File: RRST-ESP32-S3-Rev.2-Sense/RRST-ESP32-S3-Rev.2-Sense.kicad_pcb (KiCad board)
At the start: 4 copper layers, 20.1 x 39.9 mm, 35 parts, among them J1 USB_C_Receptacle_USB2.0_16P, J4 Conn_01x05_Socket, J5 Conn_01x02_Socket, J6 Conn_01x02_Socket, SW1 SW_Push, SW2 SW_Push, U1 LD1117S33TR_SOT223, U2 ESP32-S3-WROOM-1, U3 MCP2561-E-SN

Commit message: 自動配線前
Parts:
- removed CAN_BUS1, CAN_BUS2: Conn_01x04_Socket, Connector_JST:JST_GH_SM04B-GHS-TB_1x04-1MP_P1.25mm_Horizontal
- removed D7: LED, LED_SMD:LED_0603_1608Metric
- removed J4: Conn_01x05_Socket, Connector_PinSocket_2.54mm:PinSocket_1x05_P2.54mm_Horizontal
- removed R8: 0, Resistor_SMD:R_0603_1608Metric
- removed U3: MCP2561-E-SN, Package_SO:SOIC-8_3.9x4.9mm_P1.27mm
- added D8: LESD5D5.0CT1G, Diode_SMD:D_SOD-523, F.Cu at (80.6, 121.0)
- added G***: LOGO, LOGO, F.Cu at (52.1, 109.2)
- added G***: LOGO, LOGO, F.Cu at (52.1, 105.7)
- added G***: LOGO, LOGO, B.Cu at (86.2, 106.7)
- added G***: LOGO, LOGO, B.Cu at (79.1, 104.5)
- added J2: USB_C_Receptacle_USB2.0_16P, Connector_USB:USB_C_Receptacle_XKB_U262-16XN-4BVC11, F.Cu at (81.9, 131.6)
- added J3: Conn_01x22_Pin, Connector_PinHeader_2.54mm:PinHeader_1x22_P2.54mm_Vertical, B.Cu at (96.5, 78.7)
- added J7: Conn_01x04_Socket, Connector_PinHeader_2.54mm:PinHeader_1x04_P2.54mm_Vertical, F.Cu at (86.4, 116.0)
- added U4: MCP2561-E-SN, Package_SO:SOIC-8_3.9x4.9mm_P1.27mm, F.Cu at (80.2, 116.3)
- added ↓TERM: 0, Resistor_SMD:R_0805_2012Metric, F.Cu at (91.6, 105.5)
- C1: value 1uF -> 10uF
- C3: value 10uF -> 100nF
- C5: value 100nF -> 10uF
- C9: value 10uF -> 1uF
- D1: value SS14 -> LED; footprint Diode_SMD:D_SMA -> LED_SMD:LED_0603_1608Metric; moved to F.Cu
- D2: value LED -> SS14; footprint LED_SMD:LED_0603_1608Metric -> Diode_SMD:D_SMA
- D4: value LESD5D5.0CT1G -> LED; footprint Diode_SMD:D_SOD-523 -> LED_SMD:LED_0603_1608Metric
- J1: value USB_C_Receptacle_USB2.0_16P -> Conn_01x22_Pin; footprint Connector_USB:USB_C_Receptacle_XKB_U262-16XN-4BVC11 -> Connector_PinHeader_2.54mm:PinHeader_1x22_P2.54mm_Vertical; moved to B.Cu
- J5, J6: value Conn_01x02_Socket -> Conn_01x04_Socket; footprint Connector_JST:JST_PH_S2B-PH-K_1x02_P2.00mm_Horizontal -> Connector_JST:JST_XH_B4B-XH-A_1x04_P2.50mm_Vertical
- R1: value 10k -> 5.1k
- R3: value 5.1k -> 5.1K
- R5: value 5.1K -> 10k
- U1: value LD1117S33TR_SOT223 -> ESP32-S3-WROOM-1; footprint Package_TO_SOT_SMD:SOT-223-3_TabPin2 -> RF_Module:ESP32-S3-WROOM-1; moved to F.Cu
- U2: value ESP32-S3-WROOM-1 -> LD1117S33TR_SOT223; footprint RF_Module:ESP32-S3-WROOM-1 -> Package_TO_SOT_SMD:SOT-223-3_TabPin2
- moved R2 94.4 mm to (77.5, 104.9)
- moved C7 94.2 mm to (76.5, 101.1), turned to 90 degrees
- moved R1 92.5 mm to (77.5, 112.8)
- moved C5 92.4 mm to (77.5, 98.3)
- moved R4 91.4 mm to (82.1, 123.7), turned to -90 degrees
- moved R6 91.3 mm to (85.1, 98.3), turned to 180 degrees
- moved R5 90.6 mm to (84.6, 101.1), turned to -90 degrees
- moved C6 90.1 mm to (80.8, 98.3)
- moved R7 89.7 mm to (83.6, 123.8), turned to -90 degrees
- moved C4 89.6 mm to (77.5, 106.4), turned to 180 degrees
- moved C3 88.9 mm to (77.5, 107.9), turned to 180 degrees
- moved R3 88.8 mm to (80.6, 123.8), turned to -90 degrees
- moved C2 88.3 mm to (77.5, 109.4), turned to 180 degrees
- moved C1 87.9 mm to (77.5, 110.9), turned to 180 degrees
- moved C9 85.8 mm to (86.1, 101.1), turned to -90 degrees
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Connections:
- C1 pad 1: EN -> +5V
- C2 pad 1: EN -> +5V
- C4 pad 1: +5V -> 3V3
- C5 pad 1: IO0 -> 3V3
- C7 pad 1: +5V -> EN
- C8 pad 1: 3V3 -> IO0
- C9 pad 1: 3V3 -> EN
- D1 pad 1: +5V -> Net-(D1-K)
- D1 pad 2: VBUS -> 3V3
- D2 pad 1: GND -> +5V
- D2 pad 2: Net-(D2-A) -> VBUS
- D4 pad 1: VBUS -> GND
- D4 pad 2: GND -> Net-(D4-A)
- D5 pad 1: DN -> VBUS
- D6 pad 1: DP -> DN
- J5 pad 1: GPIO35 -> +5V
- J6 pad 1: GPIO36 -> +5V
- R1 pad 1: 3V3 -> +5V
- R1 pad 2: EN -> Net-(D3-A)
- R2 pad 1: +5V -> 3V3
- R2 pad 2: Net-(D2-A) -> Net-(D4-A)
- R3 pad 1: 3V3 -> Net-(J2-CC2)
- R3 pad 2: Net-(D3-A) -> GND
- R4 pad 1: Net-(J1-CC2) -> Net-(J2-CC1)
- R5 pad 1: Net-(J1-CC1) -> 3V3
- R5 pad 2: GND -> EN
- R6 pad 1: Net-(D7-K) -> Net-(D1-K)
- U1 pad 3: +5V -> EN
- U2 pad 3: EN -> +5V
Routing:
- net 3V3: track 0.00 -> 59.6 mm, vias 0 -> 2
- net GND: track 0.00 -> 54.7 mm, vias 0 -> 2
- net +5V: track 0.00 -> 24.4 mm
- net VBUS: track 0.00 -> 14.4 mm
- net DN: track 0.00 -> 3.06 mm
- net DP: track 0.00 -> 2.88 mm
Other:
- board size 20.1 x 39.9 mm -> 25.4 x 56.9 mm
- copper layers 4 -> 2
- board text added: "0"
- board text added: "1"
- board text added: "10"
- board text added: "11"
- board text added: "12"
- board text added: "13"
- board text added: "14"
- board text added: "15"
- board text added: "16"
- board text added: "17"
- board text added: "18"
- board text added: "19"
- board text added: "2"
- board text added: "20"
- board text added: "21"
- board text added: "3"
- board text added: "3.3V"
- board text added: "35"
- board text added: "36"
- board text added: "37"
- board text added: "38"
- board text added: "39"
- board text added: "3V3"
- board text added: "4"
- board text added: "40"
- board text added: "41"
- board text added: "42"
- board text added: "43"
- board text added: "44"
- board text added: "45"
- board text added: "46"
- board text added: "47"
- board text added: "48"
- board text added: "5"
- board text added: "5V"
- board text added: "6"
- board text added: "7"
- board text added: "8"
- board text added: "9"
- board text added: "BOOT"
- board text added: "GND"
- board text added: "RESET"
- board text added: "RRST-ESP32-S3 Rev.1 2026, NHK-Project, RRST"
- board text added: "RST"
- board text added: "RUN~"

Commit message: 自動配線&未配線の手直し完了
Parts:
- moved J6 0.09 mm to (91.1, 130.7)
- moved J5 0.09 mm to (91.1, 117.0)
- renumbered G*** to G***_1, G*** to G***_2, G*** to G***_3, G*** to G***_4
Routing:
- net CAN_TX: track 0.00 -> 76.0 mm, vias 0 -> 2
- net CAN_RX: track 0.00 -> 66.0 mm
- net DP: track 2.88 -> 68.1 mm, vias 0 -> 3
- net DN: track 3.06 -> 66.4 mm, vias 0 -> 3
- net +5V: track 24.4 -> 67.6 mm, vias 0 -> 1
- net IO14: track 0.00 -> 43.2 mm, vias 0 -> 2
- net IO13: track 0.00 -> 42.2 mm, vias 0 -> 1
- net EN: track 0.00 -> 39.0 mm, vias 0 -> 1
- net IO21: track 0.00 -> 38.9 mm, vias 0 -> 1
- net 3V3: track 59.6 -> 97.9 mm
- net Net-(R7-Pad1): track 0.00 -> 31.8 mm, vias 0 -> 2
- net IO12: track 0.00 -> 31.2 mm, vias 0 -> 1
- net IO10: track 0.00 -> 30.8 mm, vias 0 -> 1
- net IO0: track 0.00 -> 30.7 mm
- net IO11: track 0.00 -> 29.8 mm, vias 0 -> 2
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- added copper zone on B.Cu, net GND
- added copper zone on F.Cu, net GND
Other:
- copper layers 2 -> 4
- board text added: "RRST-ESP32-S3 Rev.2 Sense 2026, NHK-Project, RRST"
- board text added: "RUN"
- board text removed: "RRST-ESP32-S3 Rev.1 2026, NHK-Project, RRST"
- board text removed: "RUN~"

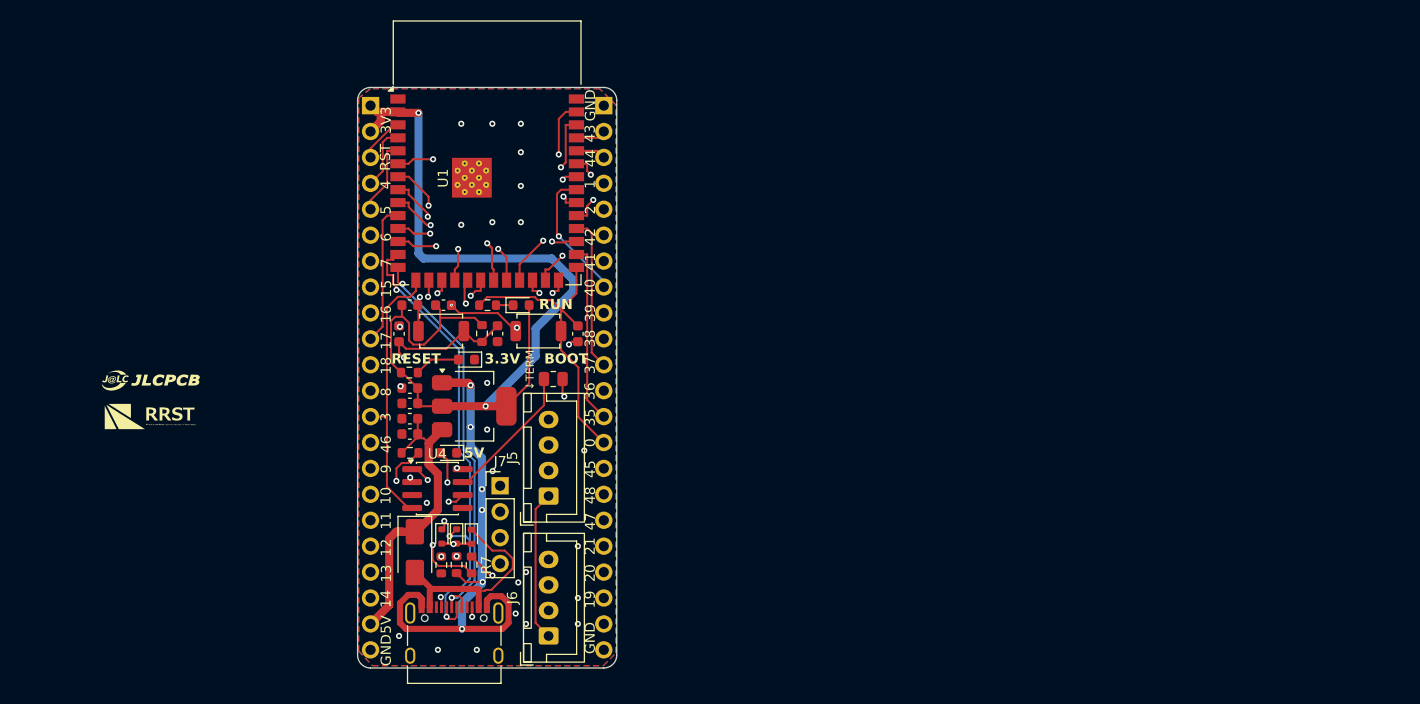
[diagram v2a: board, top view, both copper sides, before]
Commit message: マイコンにセンサ入力を増設
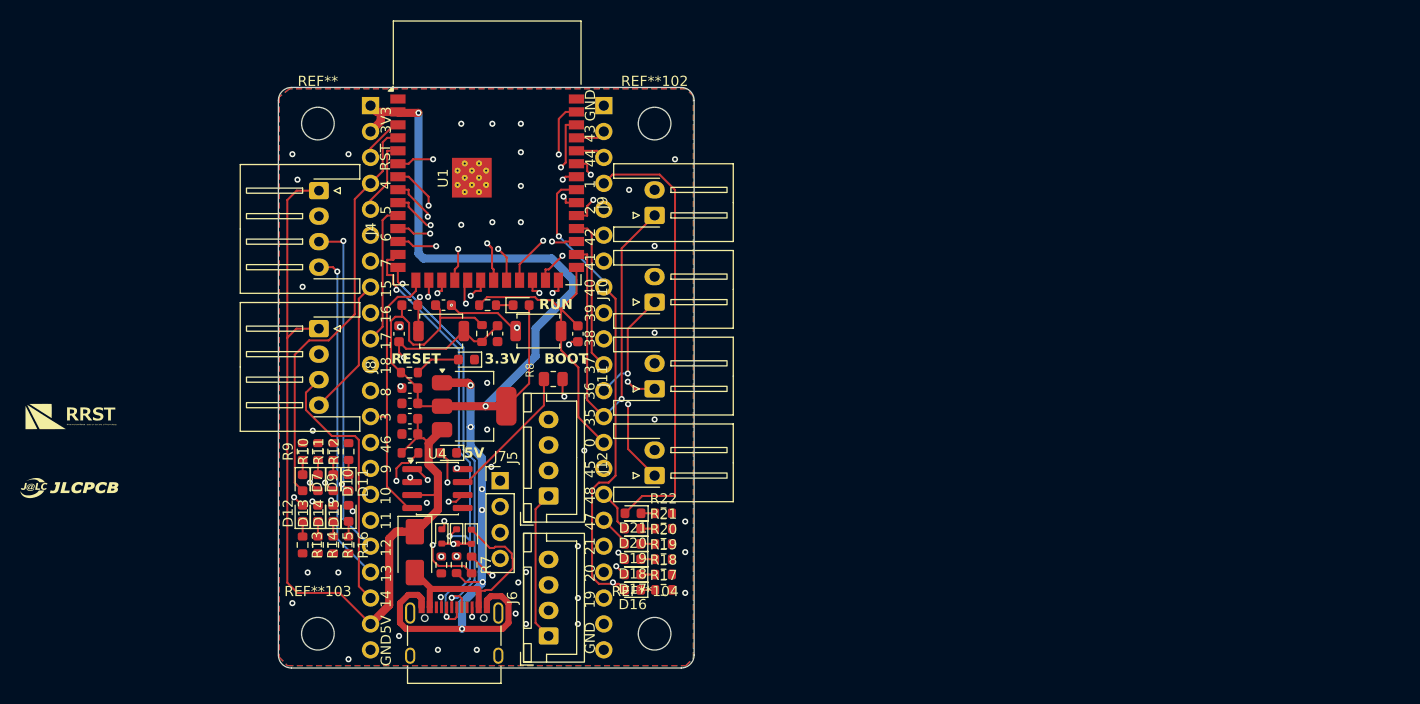
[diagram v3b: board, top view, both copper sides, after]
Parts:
- added D10: LED, LED_SMD:LED_0603_1608Metric, F.Cu at (70.0, 115.7)
- added D11: LED, LED_SMD:LED_0603_1608Metric, F.Cu at (71.5, 115.7)
- added D12: LED, LED_SMD:LED_0603_1608Metric, F.Cu at (67.0, 118.7)
- added D13: LED, LED_SMD:LED_0603_1608Metric, F.Cu at (68.5, 118.7)
- added D14: LED, LED_SMD:LED_0603_1608Metric, F.Cu at (70.0, 118.7)
- added D15: LED, LED_SMD:LED_0603_1608Metric, F.Cu at (71.5, 118.7)
- added D16: LED, LED_SMD:LED_0603_1608Metric, F.Cu at (99.3, 126.2)
- added D17: LED, LED_SMD:LED_0603_1608Metric, F.Cu at (99.3, 124.7)
- added D18: LED, LED_SMD:LED_0603_1608Metric, F.Cu at (99.3, 123.2)
- added D19: LED, LED_SMD:LED_0603_1608Metric, F.Cu at (99.3, 121.7)
- added D20: LED, LED_SMD:LED_0603_1608Metric, F.Cu at (99.3, 120.2)
- added D21: LED, LED_SMD:LED_0603_1608Metric, F.Cu at (99.4, 118.7)
- added D7: LED, LED_SMD:LED_0603_1608Metric, F.Cu at (67.0, 115.7)
- added D9: LED, LED_SMD:LED_0603_1608Metric, F.Cu at (68.5, 115.7)
- added J10: Conn_01x02_Socket, Connector_JST:JST_XH_S2B-XH-A-1_1x02_P2.50mm_Horizontal, F.Cu at (101.5, 98.0)
- added J11: Conn_01x02_Socket, Connector_JST:JST_XH_S2B-XH-A-1_1x02_P2.50mm_Horizontal, F.Cu at (101.5, 106.5)
- added J12: Conn_01x02_Socket, Connector_JST:JST_XH_S2B-XH-A-1_1x02_P2.50mm_Horizontal, F.Cu at (101.5, 115.0)
- added J4: Conn_01x04_Socket, Connector_JST:JST_XH_S4B-XH-A-1_1x04_P2.50mm_Horizontal, F.Cu at (68.6, 87.1)
- added J8: Conn_01x04_Socket, Connector_JST:JST_XH_S4B-XH-A-1_1x04_P2.50mm_Horizontal, F.Cu at (68.6, 100.6)
- added J9: Conn_01x02_Socket, Connector_JST:JST_XH_S2B-XH-A-1_1x02_P2.50mm_Horizontal, F.Cu at (101.5, 89.5)
- added R10: 330, Resistor_SMD:R_0603_1608Metric, F.Cu at (68.5, 112.6)
- added R11: 330, Resistor_SMD:R_0603_1608Metric, F.Cu at (70.0, 112.6)
- added R12: 330, Resistor_SMD:R_0603_1608Metric, F.Cu at (71.5, 112.6)
- added R13: 330, Resistor_SMD:R_0603_1608Metric, F.Cu at (67.0, 121.8)
- added R14: 330, Resistor_SMD:R_0603_1608Metric, F.Cu at (68.5, 121.8)
- added R15: 330, Resistor_SMD:R_0603_1608Metric, F.Cu at (70.0, 121.8)
- added R16: 330, Resistor_SMD:R_0603_1608Metric, F.Cu at (71.5, 121.8)
- added R17: 330, Resistor_SMD:R_0603_1608Metric, F.Cu at (102.4, 126.2)
- added R18: 330, Resistor_SMD:R_0603_1608Metric, F.Cu at (102.4, 124.7)
- added R19: 330, Resistor_SMD:R_0603_1608Metric, F.Cu at (102.4, 123.2)
- added R20: 330, Resistor_SMD:R_0603_1608Metric, F.Cu at (102.4, 121.7)
- added R21: 330, Resistor_SMD:R_0603_1608Metric, F.Cu at (102.4, 120.2)
- added R22: 330, Resistor_SMD:R_0603_1608Metric, F.Cu at (102.4, 118.7)
- added R9: 330, Resistor_SMD:R_0603_1608Metric, F.Cu at (67.0, 112.6)
- added REF**: MountingHole_3.2mm_M3, MountingHole:MountingHole_3.2mm_M3, F.Cu at (68.5, 80.5)
- added REF**102: MountingHole_3.2mm_M3, MountingHole:MountingHole_3.2mm_M3, F.Cu at (101.5, 80.5)
- added REF**103: MountingHole_3.2mm_M3, MountingHole:MountingHole_3.2mm_M3, F.Cu at (68.5, 130.5)
- added REF**104: MountingHole_3.2mm_M3, MountingHole:MountingHole_3.2mm_M3, F.Cu at (101.5, 130.5)
- moved G***_3 13.2 mm to (44.1, 116.2)
- moved G***_4 7.76 mm to (44.3, 109.2)
- moved J7 0.50 mm to (86.4, 115.5)
- renumbered ↓TERM to R8
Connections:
- net IO12 renamed ENC1_A
- net IO13 renamed ENC1_B
- net IO14 renamed ENC2_A
- net IO15 renamed ENC2_B
- C1 pad 1: +5V -> 5V0
- C2 pad 1: +5V -> 5V0
- D2 pad 1: +5V -> 5V0
- J1 pad 21: +5V -> 5V0
- J5 pad 1: +5V -> 5V0
- J6 pad 1: +5V -> 5V0
- J7 pad 1: +5V -> 5V0
- R1 pad 1: +5V -> 5V0
- U2 pad 3: +5V -> 5V0
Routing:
- net 5V0: track 0.00 -> 124.6 mm, vias 0 -> 1
- net +5V: track 67.6 -> 0.00 mm, vias 1 -> 0
- net IO1: track 11.3 -> 54.9 mm
- net IO41: track 11.1 -> 48.9 mm, vias 1 -> 2
- net IO42: track 9.34 -> 45.1 mm, vias 1 -> 2
- net IO40: track 13.1 -> 48.7 mm, vias 1 -> 2
- net IO4: track 6.19 -> 40.8 mm
- net ENC1_A: track 31.2 -> 64.6 mm, vias 1 -> 2
- net ENC1_B: track 42.2 -> 75.0 mm, vias 1 -> 2
- net IO5: track 7.46 -> 39.1 mm, vias 0 -> 1
- net IO6: track 13.6 -> 43.0 mm, vias 1 -> 2
- net ENC2_A: track 43.2 -> 69.1 mm
- net IO7: track 12.6 -> 37.3 mm, vias 1 -> 2
- net IO35: track 17.6 -> 39.4 mm, vias 0 -> 1
- net IO38: track 17.0 -> 34.0 mm, vias 1 -> 2
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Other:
- board size 25.4 x 56.9 mm -> 40.7 x 56.9 mm

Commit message: スクラップ＆ビルド
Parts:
- renumbered R8 to ↓TERM
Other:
- board text added: "+"
- board text added: "B A G 5V"
- board text added: "CAN"
- board text added: "ENC1"
- board text added: "ENC2"
- board text added: "RUN~"
- board text removed: "RUN"
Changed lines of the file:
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@@
 			(at 0 -1.43 90)
 			(layer "F.SilkS")
+			(hide yes)
 			(effects
 				(font
@@
 			(at 0 -1.43 90)
 			(layer "F.SilkS")
+			(hide yes)
 			(effects
 				(font
@@
 			(at 0 1.43 90)
 			(layer "F.Fab")
+			(hide yes)
 			(effects
 				(font
@@
 			(at 0 -1.43 0)
 			(layer "F.SilkS")
+			(hide yes)
 			(effects
 				(font
@@
 			(at 3.75 -5.1 90)
 			(layer "F.SilkS")
+			(hide yes)
 			(effects
 				(font
@@
 			(at 0 -1.43 0)
 			(layer "F.SilkS")
+			(hide yes)
 			(effects
 				(font
@@
 			(at 0 -1.43 90)
 			(layer "F.SilkS")
+			(hide yes)
 			(effects
 				(font
@@
 			(at 0 -1.43 0)
 			(layer "F.SilkS")
+			(hide yes)
 			(effects
 				(font
@@
 			(at 0 -1.43 90)
 			(layer "F.SilkS")
+			(hide yes)
 			(effects
 				(font
@@
 			(at 0 -1.43 90)
 			(layer "F.SilkS")
+			(hide yes)
 			(effects
 				(font
@@
 			(at 0 -1.43 0)
 			(layer "F.SilkS")
+			(hide yes)
 			(effects
 				(font
@@
 			(at 1.25 -5.1 90)
 			(layer "F.SilkS")
+			(hide yes)
 			(effects
 				(font
@@
 			(at 3.75 -3.55 90)
 			(layer "F.SilkS")
+			(hide yes)
 			(effects
 				(font
@@
 			(at 0 -1.43 90)
 			(layer "F.SilkS")
+			(hide yes)
 			(effects
 				(font
@@
 			(at 0 -1.43 90)
 			(layer "F.SilkS")
+			(hide yes)
 			(effects
 				(font
@@
 			(at 0 -4.15 0)
 			(layer "F.SilkS")
+			(hide yes)
 			(effects
 				(font
@@
 			(at 0 -1.43 0)
 			(layer "F.SilkS")
+			(hide yes)
 			(effects
 				(font
@@
 			(at 0 -1.43 90)
 			(layer "F.SilkS")
+			(hide yes)
 			(effects
 				(font
@@
 			(at 0 -1.43 0)
 			(layer "F.SilkS")
+			(hide yes)
 			(effects
 				(font
@@
 			(at 0 -1.43 90)
 			(layer "F.SilkS")
+			(hide yes)
 			(effects
 				(font
@@
 		(descr "Resistor SMD 0805 (2012 Metric), square (rectangular) end terminal, IPC-7351 nominal, (Body size source: IPC-SM-782 page 72, https://www.pcb-3d.com/wordpress/wp-content/uploads/ipc-sm-782a_amendment_1_and_2.pdf)")
 		(tags "resistor")
-		(property "Reference" "R8"
+		(property "Reference" "↓TERM"
 			(at -2.286 -0.8636 90)
 			(layer "F.SilkS")
@@
 			(at 0 -1.43 90)
 			(layer "F.SilkS")
+			(hide yes)
 			(effects
 				(font
@@
 			(at 3.75 -5.1 90)
 			(layer "F.SilkS")
+			(hide yes)
 			(effects
 				(font
@@
 			(at 0 -1.43 90)
 			(layer "F.SilkS")
+			(hide yes)
 			(effects
 				(font
@@
 			(at 0 -4.15 0)
 			(layer "F.SilkS")
+			(hide yes)
 			(effects
 				(font
@@
 			(at 0 -1.43 90)
 			(layer "F.SilkS")
+			(hide yes)
 			(effects
 				(font
@@
 			(at 0 -1.43 90)
 			(layer "F.SilkS")
+			(hide yes)
 			(effects
 				(font
@@
 			(at 0 -1.43 90)
 			(layer "F.SilkS")
+			(hide yes)
 			(effects
 				(font
@@
 			(at 0 -1.43 90)
 			(layer "F.SilkS")
+			(hide yes)
 			(effects
 				(font
@@
 			(at 0 -1.43 0)
 			(layer "F.SilkS")
+			(hide yes)
 			(effects
 				(font
@@
 			(at 0 -1.43 90)
 			(layer "F.SilkS")
+			(hide yes)
 			(effects
 				(font
@@
 			(at 0 -3.4 0)
 			(layer "F.SilkS")
+			(hide yes)
 			(effects
 				(font
@@
 			(at 0 -1.43 0)
 			(layer "F.SilkS")
+			(hide yes)
 			(effects
 				(font
@@
 			(at 0 -1.43 0)
 			(layer "F.SilkS")
+			(hide yes)
 			(effects
 				(font
@@
 			(at 1.25 -5.1 90)
 			(layer "F.SilkS")
+			(hide yes)
 			(effects
 				(font
@@
 			(at 0 -1.43 0)
 			(layer "F.SilkS")
+			(hide yes)
 			(effects
 				(font
@@
 			(at 1.25 -5.1 90)
 			(layer "F.SilkS")
+			(hide yes)
 			(effects
 				(font
@@
 			(at 0 -1.43 0)
 			(layer "F.SilkS")
+			(hide yes)
 			(effects
 				(font
@@
 			(at 0 -4.15 0)
 			(layer "F.SilkS")
+			(hide yes)
 			(effects
 				(font
@@
 			(at -0.925 -4.15 0)
 			(layer "F.SilkS")
+			(hide yes)
 			(effects
 				(font
@@
 			(at 0 -1.43 0)
 			(layer "F.SilkS")
+			(hide yes)
 			(effects
 				(font
@@
 			(at 0 -2.38 0)
 			(layer "F.SilkS")
+			(hide yes)
 			(effects
 				(font
@@
 			(at 3.75 -3.55 90)
 			(layer "F.SilkS")
+			(hide yes)
 			(effects
 				(font
@@
 			(at 0 -1.43 90)
 			(layer "F.SilkS")
+			(hide yes)
 			(effects
 				(font
@@
 			(at 1.25 -5.1 90)
 			(layer "F.SilkS")
+			(hide yes)
 			(effects
 				(font
@@
 		)
 	)
+	(gr_text "B  A  G  5V"
+		(at 72.4 95.6 90)
+		(layer "F.SilkS")
+		(effects
+			(font
+				(size 1 1)
+				(thickness 0.125)
+			)
+			(justify left bottom)
+		)
+	)
+	(gr_text "B  A  G  5V"
+		(at 72.6 109 90)
+		(layer "F.SilkS")
+		(effects
+			(font
+				(size 1 1)
+				(thickness 0.125)
+			)
+			(justify left bottom)
+		)
+	)
+	(gr_text "+"
+		(at 99.2 90.2 90)
+		(layer "F.SilkS")
+		(effects
+			(font
+				(size 1 1)
+				(thickness 0.125)
+			)
+			(justify left bottom)
+		)
+	)
+	(gr_text "+"
+		(at 99.2 98.7 90)
+		(layer "F.SilkS")
+		(effects
+			(font
+				(size 1 1)
+				(thickness 0.125)
+			)
+			(justify left bottom)
+		)
+	)
+	(gr_text "+"
+		(at 99.2 107.2 90)
+		(layer "F.SilkS")
+		(effects
+			(font
+				(size 1 1)
+				(thickness 0.125)
+			)
+			(justify left bottom)
+		)
+	)
+	(gr_text "+"
+		(at 99.2 115.7 90)
+		(layer "F.SilkS")
+		(effects
+			(font
+				(size 1 1)
+				(thickness 0.125)
+			)
+			(justify left bottom)
+		)
+	)
 	(gr_text "RESET"
 		(at 75.692 104.14 0)
@@
 		)
 	)
-	(gr_text "RUN"
+	(gr_text "RUN~"
 		(at 90.17 98.806 0)
 		(layer "F.SilkS" knockout)
@@
 		(layer "F.SilkS" knockout)
 		(effects
+			(font
+				(size 1 1)
+				(thickness 0.2)
+				(bold yes)
+			)
+			(justify left bottom)
+		)
+	)
+	(gr_text "ENC1"
+		(at 71 93.1 90)
+		(layer "F.SilkS" knockout)
+		(effects
+			(font
+				(size 1 1)
+				(thickness 0.2)
+				(bold yes)
+			)
+			(justify left bottom)
+		)
+	)
+	(gr_text "ENC2"
+		(at 71.1 106.5 90)
+		(layer "F.SilkS" knockout)
+		(effects
+			(font
+				(size 1 1)
+				(thickness 0.2)
+				(bold yes)
+			)
+			(justify left bottom)
+		)
+	)
+	(gr_text "CAN"
+		(at 88.1 113.7 90)
+		(layer "F.SilkS" knockout)
+		(effects
+			(font
+				(size 1 1)
+				(thickness 0.2)
+				(bold yes)
+			)
+			(justify left bottom)
+		)
+	)
+	(gr_text "CAN"
+		(at 88.1 129.1 90)
+		(layer "F.SilkS" knockout)
+		(effects
